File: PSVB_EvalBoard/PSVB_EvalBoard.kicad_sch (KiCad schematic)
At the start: 458 parts, among them J1 PIN2, J10 PIN20, J11 PIN12_2x6, J12 PIN20, J13 PIN6_2x3, J29 PIN6_2x3, J3 PIN20, J30 PIN6_2x3, J31 PIN6_2x3, J4 PIN20, J5 PIN20, J6 PIN20, J7 PIN20, J8 PIN20, J9 PIN20, Q1 S9013, U1 SGM2036-ADJ, U12 STM32F429ZETx, U13 CH395Q, U14 CH395Q, U16 MPU6050, U2 SGM2036-ADJ, U3 93LC56BT-IOT, U3 SGM2036-ADJ, U4 INA240A1PWR, U5 INA240A1PWR, U5 W25Q128JVSIQ, U6 24LC64ISN, U6 TM7707, U7 REF3030, U8 REF3025, U9 REF3012, X1 2.4576Mhz, X2 12Mhz_Passive_3225, X3 16Mhz_Passive_3225, X4 30Mhz_3225, X5 30Mhz_3225

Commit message: Finished PCB layout.
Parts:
- added R42: 0603 47K/1%, Resistor_SMD:R_0603_1608Metric_Pad0.98x0.95mm_HandSolder, symbol Device:R
- R42: value 0603 1K/1% -> 0603 47K/1%
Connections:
- net BTB_PB2 is gone; now on net VSS: BTB100x1.167
- net PF9 is gone; now on net STM32_USB_ID: J3.16
- net +3V3: now also R42.2, R42.2, R42.2, R42.2, R42.2, R42.2
- net OPAMP1_IN: now also J24.3
- net OPAMP1_IP: now also J24.1
- net PC10: now also R42.1
- net PC11: now also R42.1
- net PC8: now also R42.1
- net PC9: now also R42.1
- net PD2: now also R42.1
- net PD3: now also R42.1
- net VSS: now also J24.2
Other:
- moved on the sheet: J24, R42, SD1

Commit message: Project finished.
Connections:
- net VSS: now also BTB100x1.69; no longer BTB100x1.167, J9.10
- new net BTB_PB2: BTB100x1.167, J9.10
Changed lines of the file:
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@@
     (stroke (width 0) (type default))
   )
-  (wire (pts (xy 612.14 351.79) (xy 629.92 351.79))
+  (wire (pts (xy 612.14 351.79) (xy 635 351.79))
     (stroke (width 0) (type default))
   )
@@
     (stroke (width 0) (type default))
   )
-  (wire (pts (xy 698.5 488.95) (xy 698.5 504.19))
-    (stroke (width 0) (type default))
-  )
   (wire (pts (xy 674.37 499.11) (xy 693.42 499.11))
     (stroke (width 0) (type default))
@@
     (stroke (width 0) (type default))
   )
-  (wire (pts (xy 674.37 488.95) (xy 698.5 488.95))
+  (wire (pts (xy 674.37 488.95) (xy 688.34 488.95))
     (stroke (width 0) (type default))
   )
@@
     (stroke (width 0) (type default))
   )
-  (wire (pts (xy 713.74 297.18) (xy 731.52 297.18))
-    (stroke (width 0) (type default))
-  )
   (wire (pts (xy 858.52 281.94) (xy 858.52 278.13))
     (stroke (width 0) (type default))
@@
     (effects (font (size 1.27 1.27)) (justify left bottom))
   )
-  (label "BTB_PB2" (at 713.74 297.18 0) (fields_autoplaced)
-    (effects (font (size 1.27 1.27)) (justify left bottom))
-  )
   (label "AKINA_KEY_B" (at 826.135 463.55 0) (fields_autoplaced)
     (effects (font (size 1.27 1.27)) (justify left bottom))
@@
     )
   )
+  (symbol (lib_id "power:VSS") (at 635 351.79 270) (unit 1)
+    (in_bom yes) (on_board yes) (dnp no)
+    (property "Reference" "#PWR0170" (at 631.19 351.79 0)
+      (effects (font (size 1.27 1.27)) hide)
+    )
+    (property "Value" "VSS" (at 637.54 351.79 90)
+      (effects (font (size 1.27 1.27)) (justify left))
+    )
+    (property "Footprint" "" (at 635 351.79 0)
+      (effects (font (size 1.27 1.27)) hide)
+    )
+    (property "Datasheet" "" (at 635 351.79 0)
+      (effects (font (size 1.27 1.27)) hide)
+    )
+    (pin "1")
+    (instances
+      (project "PSVB_EvalBoard"
+        (path "/f2b0a56f-d786-40ff-9774-78e3f95871c8"
+          (reference "#PWR0170") (unit 1)
+        )
+      )
+    )
+  )
   (symbol (lib_id "power:VSS") (at 232.41 326.39 270) (unit 1)
     (in_bom yes) (on_board yes) (dnp no)
@@
         )
       )
-    )
-  )
-  (symbol (lib_id "power:VSS") (at 698.5 504.19 180) (unit 1)
-    (in_bom yes) (on_board yes) (dnp no)
-    (property "Reference" "#PWR0170" (at 698.5 500.38 0)
-      (effects (font (size 1.27 1.27)) hide)
-    )
-    (property "Value" "VSS" (at 698.5 508 0)
-      (effects (font (size 1.27 1.27)))
-    )
-    (property "Footprint" "" (at 698.5 504.19 0)
-      (effects (font (size 1.27 1.27)) hide)
-    )
-    (property "Datasheet" "" (at 698.5 504.19 0)
-      (effects (font (size 1.27 1.27)) hide)
-    )
-    (pin "1")
-    (instances
-      (project "PSVB_EvalBoard"
-        (path "/f2b0a56f-d786-40ff-9774-78e3f95871c8"
-          (reference "#PWR0170") (unit 1)
-        )
-      )

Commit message: Fix some errors.
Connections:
- net VREF_3.3V is gone; now on net +3V3: U12.32 (VREF+)
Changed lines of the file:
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@@
     (stroke (width 0) (type default))
   )
+  (wire (pts (xy 378.46 317.5) (xy 378.46 320.04))
+    (stroke (width 0) (type default))
+  )
   (wire (pts (xy 580.39 194.31) (xy 603.25 194.31))
     (stroke (width 0) (type default))
@@
     (stroke (width 0) (type default))
   )
-  (wire (pts (xy 386.08 320.04) (xy 407.67 320.04))
+  (wire (pts (xy 378.46 320.04) (xy 407.67 320.04))
     (stroke (width 0) (type default))
   )
@@
         )
       )
+    )
+  )
+  (symbol (lib_id "power:+3.3V") (at 378.46 317.5 0) (unit 1)
+    (in_bom yes) (on_board yes) (dnp no)
+    (property "Reference" "#PWR0163" (at 378.46 321.31 0)
+      (effects (font (size 1.27 1.27)) hide)
+    )
+    (property "Value" "+3.3V" (at 378.841 313.1058 0)
+      (effects (font (size 1.27 1.27)))
+    )
+    (property "Footprint" "" (at 378.46 317.5 0)
+      (effects (font (size 1.27 1.27)) hide)
+    )
+    (property "Datasheet" "" (at 378.46 317.5 0)
+      (effects (font (size 1.27 1.27)) hide)
+    )
+    (pin "1")
+    (instances
+      (project "PutuoEvalBoard_V2"
+        (path "/a62609cd-29b7-4918-b97d-7b2404ba61cf"
+          (reference "#PWR0163") (unit 1)
+        )
+      )
+      (project "PSVB_EvalBoard"
+        (path "/f2b0a56f-d786-40ff-9774-78e3f95871c8"
+          (reference "#PWR0273") (unit 1)
+        )
+      )

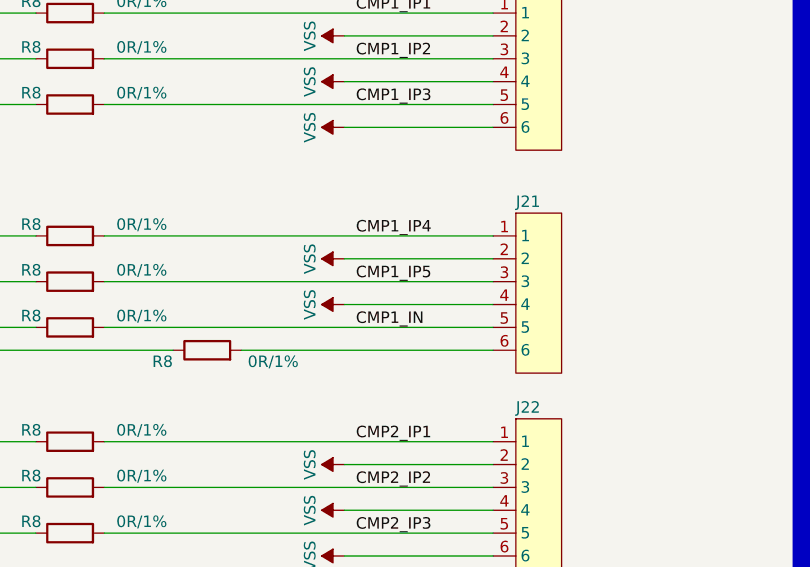
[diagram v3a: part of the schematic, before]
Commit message: Finished the bottom silkscreen.
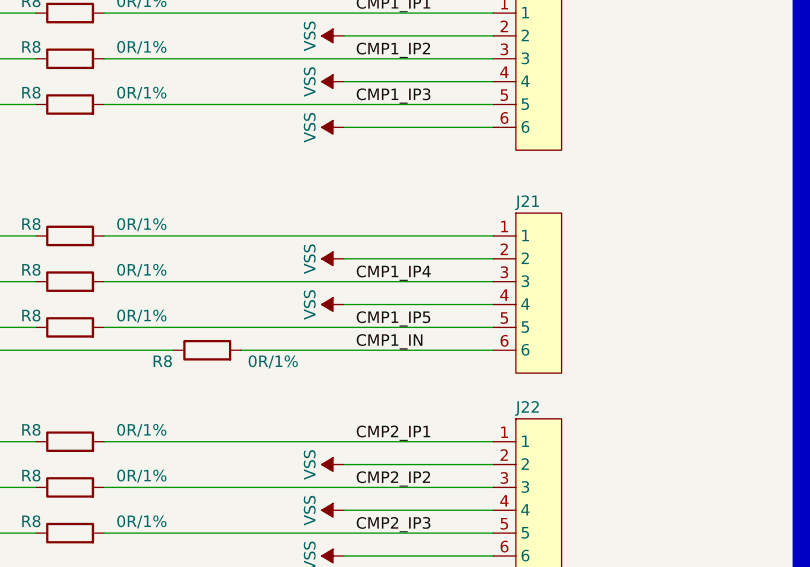
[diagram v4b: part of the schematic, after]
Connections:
- net CMP1_IN: now also J21.6, R8.2; no longer J21.5, R8.2
- net CMP1_IP4: now also J21.3, R8.2; no longer J21.1, R8.2
- net CMP1_IP5: now also J21.5, R8.2; no longer J21.3, R8.2
- new net: J21.1, R8.2
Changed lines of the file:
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@@
     (effects (font (size 1.27 1.27) (color 0 0 0 1)) (justify left bottom))
+  )
+  (label "CMP1_IP5" (at 1127.76 397.51 0) (fields_autoplaced)
+    (effects (font (size 1.27 1.27)) (justify left bottom))
   )
   (label "PC12" (at 485.14 424.18 0) (fields_autoplaced)
@@
     (effects (font (size 1.27 1.27)) (justify left bottom))
   )
-  (label "CMP1_IP5" (at 1127.76 392.43 0) (fields_autoplaced)
-    (effects (font (size 1.27 1.27)) (justify left bottom))
-  )
   (label "EXP_PIN11" (at 739.14 481.33 0) (fields_autoplaced)
     (effects (font (size 1.27 1.27)) (justify left bottom))
@@
     (effects (font (size 1.27 1.27)) (justify left bottom))
   )
+  (label "CMP1_IP4" (at 1127.76 392.43 0) (fields_autoplaced)
+    (effects (font (size 1.27 1.27)) (justify left bottom))
+  )
   (label "AKINA_KEY_D" (at 826.135 482.6 0) (fields_autoplaced)
     (effects (font (size 1.27 1.27)) (justify left bottom))
@@
     (effects (font (size 1.27 1.27)) (justify left bottom))
   )
+  (label "CMP1_IN" (at 1127.76 400.05 0) (fields_autoplaced)
+    (effects (font (size 1.27 1.27)) (justify left bottom))
+  )
   (label "STM32_KEY1" (at 166.37 774.7 0) (fields_autoplaced)
     (effects (font (size 1.27 1.27)) (justify left bottom))
@@
     (effects (font (size 1.27 1.27)) (justify left bottom))
   )
-  (label "CMP1_IP4" (at 1127.76 387.35 0) (fields_autoplaced)
-    (effects (font (size 1.27 1.27)) (justify left bottom))
-  )
   (label "TP29" (at 551.18 300.99 0) (fields_autoplaced)
     (effects (font (size 1.27 1.27)) (justify left bottom))
@@
     (effects (font (size 1.27 1.27)) (justify left bottom))
   )
-  (label "CMP1_IN" (at 1127.76 397.51 0) (fields_autoplaced)
-    (effects (font (size 1.27 1.27)) (justify left bottom))
-  )
